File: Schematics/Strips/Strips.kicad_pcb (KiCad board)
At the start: 2 copper layers, 21 x 99.5 mm, 46 parts, among them J1 Conn_01x04

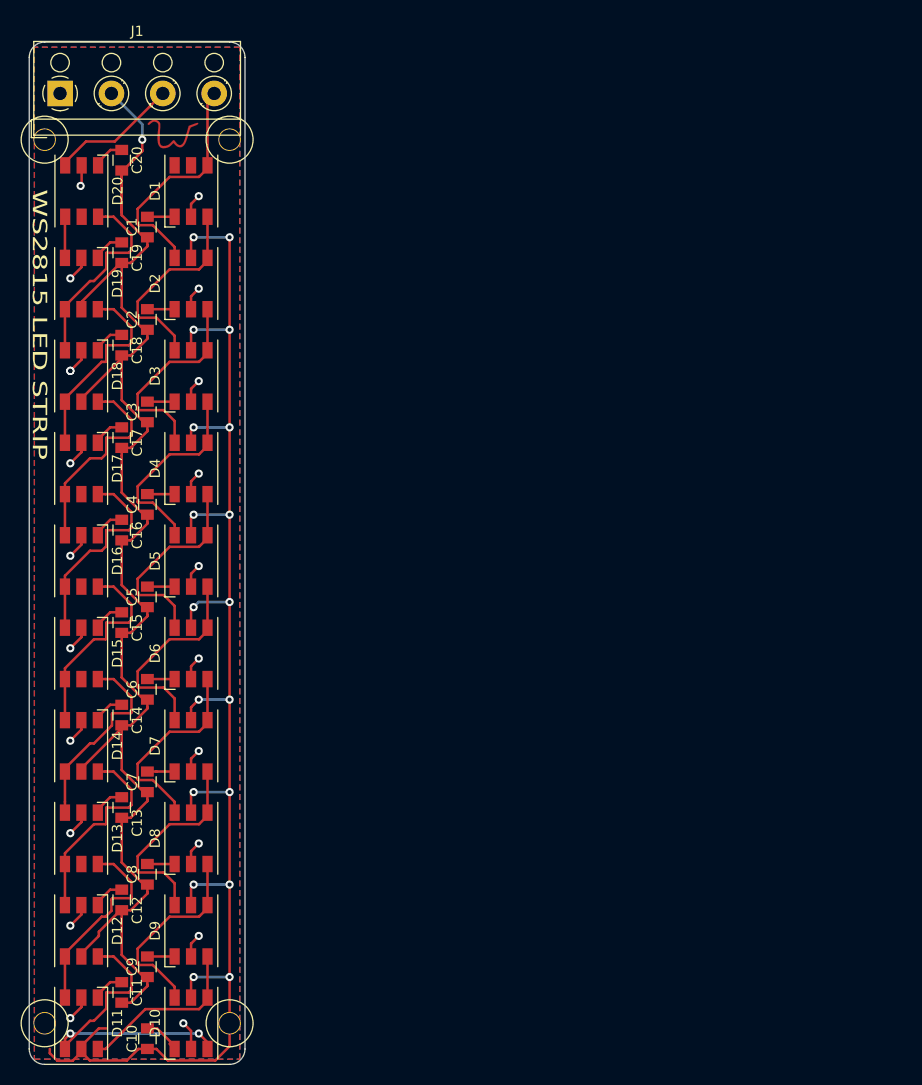
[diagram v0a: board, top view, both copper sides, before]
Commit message: Added stencil
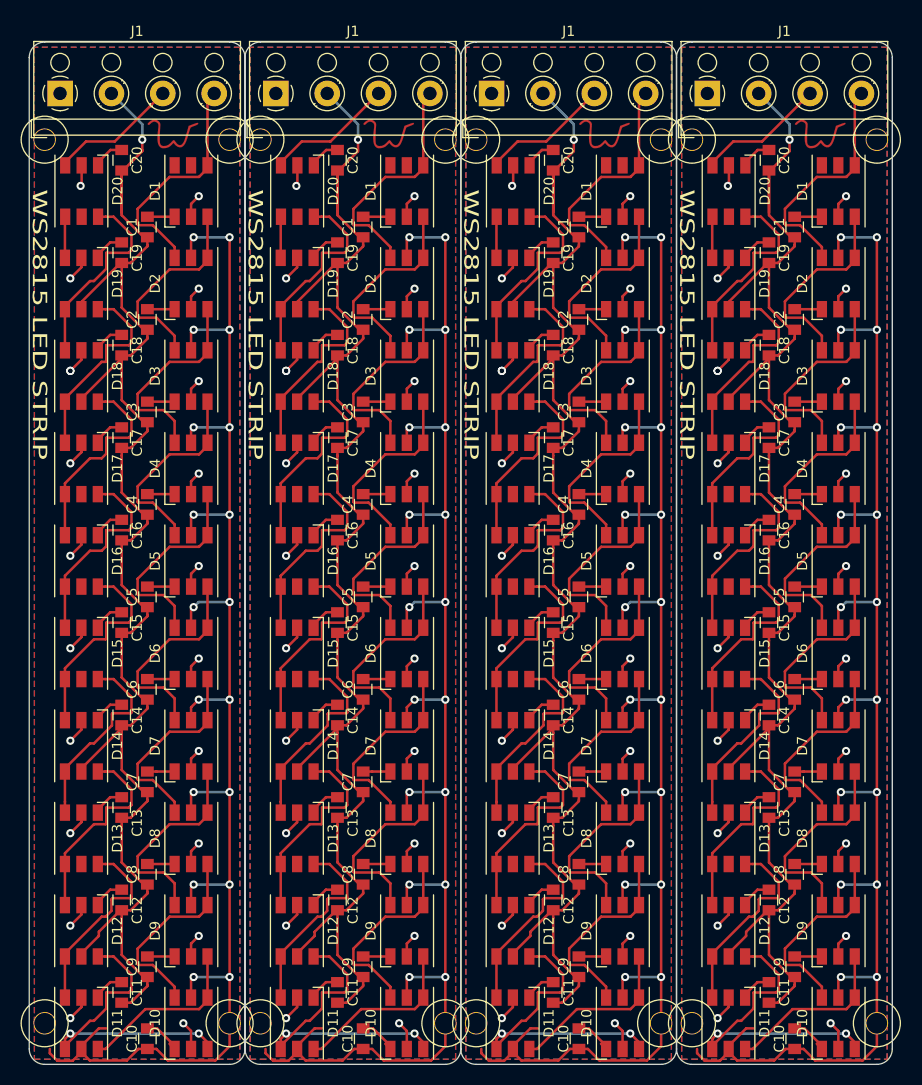
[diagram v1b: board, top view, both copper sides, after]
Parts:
- added C1: 100nF, Capacitors_SMD:C_0805, F.Cu at (204.5, 62.5)
- added C1: 100nF, Capacitors_SMD:C_0805, F.Cu at (183.5, 62.5)
- added C1: 100nF, Capacitors_SMD:C_0805, F.Cu at (162.5, 62.5)
- added C10: 100nF, Capacitors_SMD:C_0805, F.Cu at (183.5, 141.5)
- added C10: 100nF, Capacitors_SMD:C_0805, F.Cu at (204.5, 141.5)
- added C10: 100nF, Capacitors_SMD:C_0805, F.Cu at (162.5, 141.5)
- added C11: 100nF, Capacitors_SMD:C_0805, F.Cu at (181.0, 137.0)
- added C11: 100nF, Capacitors_SMD:C_0805, F.Cu at (202.0, 137.0)
- added C11: 100nF, Capacitors_SMD:C_0805, F.Cu at (160.0, 137.0)
- added C12: 100nF, Capacitors_SMD:C_0805, F.Cu at (202.0, 128.0)
- added C12: 100nF, Capacitors_SMD:C_0805, F.Cu at (181.0, 128.0)
- added C12: 100nF, Capacitors_SMD:C_0805, F.Cu at (160.0, 128.0)
- added C13: 100nF, Capacitors_SMD:C_0805, F.Cu at (181.0, 119.0)
- added C13: 100nF, Capacitors_SMD:C_0805, F.Cu at (202.0, 119.0)
- added C13: 100nF, Capacitors_SMD:C_0805, F.Cu at (160.0, 119.0)
- added C14: 100nF, Capacitors_SMD:C_0805, F.Cu at (181.0, 110.0)
- added C14: 100nF, Capacitors_SMD:C_0805, F.Cu at (202.0, 110.0)
- added C14: 100nF, Capacitors_SMD:C_0805, F.Cu at (160.0, 110.0)
- added C15: 100nF, Capacitors_SMD:C_0805, F.Cu at (181.0, 101.0)
- added C15: 100nF, Capacitors_SMD:C_0805, F.Cu at (202.0, 101.0)
- added C15: 100nF, Capacitors_SMD:C_0805, F.Cu at (160.0, 101.0)
- added C16: 100nF, Capacitors_SMD:C_0805, F.Cu at (202.0, 92.0)
- added C16: 100nF, Capacitors_SMD:C_0805, F.Cu at (181.0, 92.0)
- added C16: 100nF, Capacitors_SMD:C_0805, F.Cu at (160.0, 92.0)
- added C17: 100nF, Capacitors_SMD:C_0805, F.Cu at (202.0, 83.0)
- added C17: 100nF, Capacitors_SMD:C_0805, F.Cu at (181.0, 83.0)
- added C17: 100nF, Capacitors_SMD:C_0805, F.Cu at (160.0, 83.0)
- added C18: 100nF, Capacitors_SMD:C_0805, F.Cu at (181.0, 74.0)
- added C18: 100nF, Capacitors_SMD:C_0805, F.Cu at (202.0, 74.0)
- added C18: 100nF, Capacitors_SMD:C_0805, F.Cu at (160.0, 74.0)
- added C19: 100nF, Capacitors_SMD:C_0805, F.Cu at (181.0, 65.0)
- added C19: 100nF, Capacitors_SMD:C_0805, F.Cu at (202.0, 65.0)
- added C19: 100nF, Capacitors_SMD:C_0805, F.Cu at (160.0, 65.0)
- added C2: 100nF, Capacitors_SMD:C_0805, F.Cu at (183.5, 71.5)
- added C2: 100nF, Capacitors_SMD:C_0805, F.Cu at (204.5, 71.5)
- added C2: 100nF, Capacitors_SMD:C_0805, F.Cu at (162.5, 71.5)
- added C20: 100nF, Capacitors_SMD:C_0805, F.Cu at (181.0, 56.0)
- added C20: 100nF, Capacitors_SMD:C_0805, F.Cu at (202.0, 56.0)
- added C20: 100nF, Capacitors_SMD:C_0805, F.Cu at (160.0, 56.0)
- added C3: 100nF, Capacitors_SMD:C_0805, F.Cu at (183.5, 80.5)
- added C3: 100nF, Capacitors_SMD:C_0805, F.Cu at (204.5, 80.5)
- added C3: 100nF, Capacitors_SMD:C_0805, F.Cu at (162.5, 80.5)
- added C4: 100nF, Capacitors_SMD:C_0805, F.Cu at (204.5, 89.5)
- added C4: 100nF, Capacitors_SMD:C_0805, F.Cu at (183.5, 89.5)
- added C4: 100nF, Capacitors_SMD:C_0805, F.Cu at (162.5, 89.5)
- added C5: 100nF, Capacitors_SMD:C_0805, F.Cu at (204.5, 98.5)
- added C5: 100nF, Capacitors_SMD:C_0805, F.Cu at (183.5, 98.5)
- added C5: 100nF, Capacitors_SMD:C_0805, F.Cu at (162.5, 98.5)
- added C6: 100nF, Capacitors_SMD:C_0805, F.Cu at (183.5, 107.5)
- added C6: 100nF, Capacitors_SMD:C_0805, F.Cu at (204.5, 107.5)
- added C6: 100nF, Capacitors_SMD:C_0805, F.Cu at (162.5, 107.5)
- added C7: 100nF, Capacitors_SMD:C_0805, F.Cu at (183.5, 116.5)
- added C7: 100nF, Capacitors_SMD:C_0805, F.Cu at (204.5, 116.5)
- added C7: 100nF, Capacitors_SMD:C_0805, F.Cu at (162.5, 116.5)
- added C8: 100nF, Capacitors_SMD:C_0805, F.Cu at (204.5, 125.5)
- added C8: 100nF, Capacitors_SMD:C_0805, F.Cu at (183.5, 125.5)
- added C8: 100nF, Capacitors_SMD:C_0805, F.Cu at (162.5, 125.5)
- added C9: 100nF, Capacitors_SMD:C_0805, F.Cu at (183.5, 134.5)
- added C9: 100nF, Capacitors_SMD:C_0805, F.Cu at (204.5, 134.5)
- added C9: 100nF, Capacitors_SMD:C_0805, F.Cu at (162.5, 134.5)
- added D1: WS2813, LEDs:LED_WS2812-PLCC6, F.Cu at (187.8, 59.0)
- added D1: WS2813, LEDs:LED_WS2812-PLCC6, F.Cu at (208.8, 59.0)
- added D1: WS2813, LEDs:LED_WS2812-PLCC6, F.Cu at (166.8, 59.0)
- added D10: WS2813, LEDs:LED_WS2812-PLCC6, F.Cu at (187.8, 140.0)
- added D10: WS2813, LEDs:LED_WS2812-PLCC6, F.Cu at (208.8, 140.0)
- added D10: WS2813, LEDs:LED_WS2812-PLCC6, F.Cu at (166.8, 140.0)
- added D11: WS2813, LEDs:LED_WS2812-PLCC6, F.Cu at (177.1, 140.0)
- added D11: WS2813, LEDs:LED_WS2812-PLCC6, F.Cu at (198.1, 140.0)
- added D11: WS2813, LEDs:LED_WS2812-PLCC6, F.Cu at (156.1, 140.0)
- added D12: WS2813, LEDs:LED_WS2812-PLCC6, F.Cu at (177.1, 131.0)
- added D12: WS2813, LEDs:LED_WS2812-PLCC6, F.Cu at (198.1, 131.0)
- added D12: WS2813, LEDs:LED_WS2812-PLCC6, F.Cu at (156.1, 131.0)
- added D13: WS2813, LEDs:LED_WS2812-PLCC6, F.Cu at (177.1, 122.0)
- added D13: WS2813, LEDs:LED_WS2812-PLCC6, F.Cu at (198.1, 122.0)
- added D13: WS2813, LEDs:LED_WS2812-PLCC6, F.Cu at (156.1, 122.0)
- added D14: WS2813, LEDs:LED_WS2812-PLCC6, F.Cu at (177.1, 113.0)
- added D14: WS2813, LEDs:LED_WS2812-PLCC6, F.Cu at (198.1, 113.0)
- added D14: WS2813, LEDs:LED_WS2812-PLCC6, F.Cu at (156.1, 113.0)
- added D15: WS2813, LEDs:LED_WS2812-PLCC6, F.Cu at (177.1, 104.0)
- added D15: WS2813, LEDs:LED_WS2812-PLCC6, F.Cu at (198.1, 104.0)
- added D15: WS2813, LEDs:LED_WS2812-PLCC6, F.Cu at (156.1, 104.0)
- added D16: WS2813, LEDs:LED_WS2812-PLCC6, F.Cu at (198.1, 95.0)
- added D16: WS2813, LEDs:LED_WS2812-PLCC6, F.Cu at (177.1, 95.0)
- added D16: WS2813, LEDs:LED_WS2812-PLCC6, F.Cu at (156.1, 95.0)
- added D17: WS2813, LEDs:LED_WS2812-PLCC6, F.Cu at (198.1, 86.0)
- added D17: WS2813, LEDs:LED_WS2812-PLCC6, F.Cu at (177.1, 86.0)
- added D17: WS2813, LEDs:LED_WS2812-PLCC6, F.Cu at (156.1, 86.0)
- added D18: WS2813, LEDs:LED_WS2812-PLCC6, F.Cu at (198.1, 77.0)
- added D18: WS2813, LEDs:LED_WS2812-PLCC6, F.Cu at (177.1, 77.0)
- added D18: WS2813, LEDs:LED_WS2812-PLCC6, F.Cu at (156.1, 77.0)
- added D19: WS2813, LEDs:LED_WS2812-PLCC6, F.Cu at (198.1, 68.0)
- added D19: WS2813, LEDs:LED_WS2812-PLCC6, F.Cu at (177.1, 68.0)
- added D19: WS2813, LEDs:LED_WS2812-PLCC6, F.Cu at (156.1, 68.0)
- added D2: WS2813, LEDs:LED_WS2812-PLCC6, F.Cu at (187.8, 68.0)
- added D2: WS2813, LEDs:LED_WS2812-PLCC6, F.Cu at (208.8, 68.0)
- added D2: WS2813, LEDs:LED_WS2812-PLCC6, F.Cu at (166.8, 68.0)
- added D20: WS2813, LEDs:LED_WS2812-PLCC6, F.Cu at (177.1, 59.0)
- added D20: WS2813, LEDs:LED_WS2812-PLCC6, F.Cu at (198.1, 59.0)
- added D20: WS2813, LEDs:LED_WS2812-PLCC6, F.Cu at (156.1, 59.0)
- added D3: WS2813, LEDs:LED_WS2812-PLCC6, F.Cu at (187.8, 77.0)
- added D3: WS2813, LEDs:LED_WS2812-PLCC6, F.Cu at (208.8, 77.0)
- added D3: WS2813, LEDs:LED_WS2812-PLCC6, F.Cu at (166.8, 77.0)
- added D4: WS2813, LEDs:LED_WS2812-PLCC6, F.Cu at (187.8, 86.0)
- added D4: WS2813, LEDs:LED_WS2812-PLCC6, F.Cu at (208.8, 86.0)
- added D4: WS2813, LEDs:LED_WS2812-PLCC6, F.Cu at (166.8, 86.0)
- added D5: WS2813, LEDs:LED_WS2812-PLCC6, F.Cu at (187.8, 95.0)
- added D5: WS2813, LEDs:LED_WS2812-PLCC6, F.Cu at (208.8, 95.0)
- added D5: WS2813, LEDs:LED_WS2812-PLCC6, F.Cu at (166.8, 95.0)
- added D6: WS2813, LEDs:LED_WS2812-PLCC6, F.Cu at (208.8, 104.0)
- added D6: WS2813, LEDs:LED_WS2812-PLCC6, F.Cu at (187.8, 104.0)
- added D6: WS2813, LEDs:LED_WS2812-PLCC6, F.Cu at (166.8, 104.0)
- added D7: WS2813, LEDs:LED_WS2812-PLCC6, F.Cu at (208.8, 113.0)
- added D7: WS2813, LEDs:LED_WS2812-PLCC6, F.Cu at (187.8, 113.0)
- added D7: WS2813, LEDs:LED_WS2812-PLCC6, F.Cu at (166.8, 113.0)
- added D8: WS2813, LEDs:LED_WS2812-PLCC6, F.Cu at (187.8, 122.0)
- added D8: WS2813, LEDs:LED_WS2812-PLCC6, F.Cu at (208.8, 122.0)
- added D8: WS2813, LEDs:LED_WS2812-PLCC6, F.Cu at (166.8, 122.0)
- added D9: WS2813, LEDs:LED_WS2812-PLCC6, F.Cu at (187.8, 131.0)
- added D9: WS2813, LEDs:LED_WS2812-PLCC6, F.Cu at (208.8, 131.0)
- added D9: WS2813, LEDs:LED_WS2812-PLCC6, F.Cu at (166.8, 131.0)
- added J1: Conn_01x04, TerminalBlock_RND:TerminalBlock_RND_205-00003_Pitch5.00mm, F.Cu at (196.0, 49.5)
- added J1: Conn_01x04, TerminalBlock_RND:TerminalBlock_RND_205-00003_Pitch5.00mm, F.Cu at (175.0, 49.5)
- added J1: Conn_01x04, TerminalBlock_RND:TerminalBlock_RND_205-00003_Pitch5.00mm, F.Cu at (154.0, 49.5)
- added REF**: 1pin, Connectors:1pin, F.Cu at (173.5, 54.0)
- added REF**: 1pin, Connectors:1pin, F.Cu at (170.5, 54.0)
- added REF**: 1pin, Connectors:1pin, F.Cu at (152.5, 140.0)
- added REF**: 1pin, Connectors:1pin, F.Cu at (170.5, 140.0)
- added REF**: 1pin, Connectors:1pin, F.Cu at (191.5, 54.0)
- added REF**: 1pin, Connectors:1pin, F.Cu at (173.5, 140.0)
- added REF**: 1pin, Connectors:1pin, F.Cu at (194.5, 54.0)
- added REF**: 1pin, Connectors:1pin, F.Cu at (212.5, 54.0)
- added REF**: 1pin, Connectors:1pin, F.Cu at (194.5, 140.0)
- added REF**: 1pin, Connectors:1pin, F.Cu at (212.5, 140.0)
- added REF**: 1pin, Connectors:1pin, F.Cu at (191.5, 140.0)
- added REF**: 1pin, Connectors:1pin, F.Cu at (152.5, 54.0)
- added Ref**: Val**, NFCBuisness:W, F.Cu at (186.0, 54.5)
- added Ref**: Val**, NFCBuisness:W, F.Cu at (207.0, 54.5)
- added Ref**: Val**, NFCBuisness:W, F.Cu at (165.0, 54.5)
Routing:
- net VSS: track 297.4 -> 1189.4 mm, vias 19 -> 76
- net +12V: track 47.7 -> 190.6 mm, vias 21 -> 84
- net Mid: track 31.5 -> 126.1 mm, vias 2 -> 8
- net DIN: track 23.5 -> 94.0 mm
- net Net-(D4-Pad3): track 20.4 -> 81.7 mm
- net Net-(D7-Pad3): track 20.4 -> 81.7 mm
- net Net-(D5-Pad3): track 20.4 -> 81.7 mm
- net Net-(D2-Pad3): track 20.4 -> 81.7 mm
- net Net-(D1-Pad3): track 20.0 -> 80.1 mm
- net Net-(D16-Pad3): track 19.9 -> 79.6 mm
- net Net-(D15-Pad3): track 19.9 -> 79.6 mm
- net Net-(D14-Pad3): track 19.9 -> 79.6 mm
- net Net-(D12-Pad3): track 19.9 -> 79.6 mm
- net Net-(D10-Pad6): track 19.8 -> 79.2 mm
- net Net-(D6-Pad3): track 19.8 -> 79.2 mm
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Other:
- board size 21 x 99.5 mm -> 84 x 99.5 mm
